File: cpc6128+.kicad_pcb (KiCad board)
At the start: 2 copper layers, 284 x 140.5 mm, 194 parts, among them IC101 AMS40489, IC102 z80_6128, IC103 SED9420Cac, IC104 UPD765AC-2, IC105 74LS38, IC106 74LS38, IC107 74HC14, IC108 MC74HC4051N, IC109 LA6393D, IC110 41464, IC111 41464, IC112 41464, IC113 41464, IC114 AY38912, IC115 AMS40464, IC116 74HCT02, J101 rj12, J102 audio/video, J103 Jack audio, J104 Jack Power, Q101 KTC1815Y, Q103 KTC1815Y, Q104 KTC1815Y, Q105 KTC1815Y, Q106 KTC1815Y, Q107 KTC1815Y, SW1 SW_DIP_x01, X181 40MhZ

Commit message: more accurate on pins definition, power, centronic 36, jack, and some wiring
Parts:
- added C151: 47uF 16V, Capacitor_THT:CP_Radial_D5.0mm_P2.50mm, F.Cu at (218.0, 138.2)
- added L101: ESD-R-12C, cpc6128+:L_Toroid_Vertical_L17_P17, F.Cu at (252.0, 49.2)
- added NC?: nc_db9, cpc6128+:nc_db9, F.Cu at (36.8, 98.5)
- added NC?: nc_db25_db15, cpc6128+:nc_db25_db15, F.Cu at (35.8, 63.0)
- added R210: 470k, Resistor_THT:R_Axial_DIN0207_L6.3mm_D2.5mm_P10.16mm_Horizontal, F.Cu at (243.8, 145.0)
- C130, C139: footprint Capacitor_THT:CP_Radial_D8.0mm_P2.50mm -> Capacitor_THT:CP_Radial_D8.0mm_P5.00mm
- C135: footprint Capacitor_THT:CP_Radial_D5.0mm_P2.50mm -> Capacitor_THT:CP_Radial_D8.0mm_P5.00mm
- CD104: footprint Connector_PinSocket_2.54mm:PinSocket_2x13_P2.54mm_Vertical -> Connector_IDC:IDC-Header_2x13_P2.54mm_Vertical
- IC114: footprint Package_DIP:DIP-28_W7.62mm -> Package_DIP:DIP-28_W15.24mm
- J103: footprint Connector_Audio:Jack_3.5mm_CUI_SJ1-3533NG_Horizontal -> cpc6128+:Jack_6128
- J104: value Jack Power -> POWER_JACK_6128; footprint Connector_BarrelJack:BarrelJack_CUI_PJ-102AH_Horizontal -> cpc6128+:power_jack_6128
- L104: footprint Inductor_THT:L_Toroid_Horizontal_D7.8mm_P13.00mm_Diameter9-5mm_Amidon-T30 -> cpc6128+:L_Toroid_Vertical_L13_P13
- R182: value pont -> 680
- SW1: footprint Connector_PinSocket_1.00mm:PinSocket_1x02_P1.00mm_Vertical -> Connector_PinHeader_2.54mm:PinHeader_1x02_P2.54mm_Vertical
- X181: value 40MhZ -> 40 MHz; footprint Oscillator:Oscillator_DIP-8 -> Oscillator:Oscillator_DIP-14
- moved VR101 48.6 mm to (223.5, 139.0)
- moved J104 11.4 mm to (225.2, 24.8), turned to 0 degrees
- moved L104 8.88 mm to (224.8, 44.0)
- moved D124 7.85 mm to (43.8, 92.5)
- moved NC? 7.81 mm to (37.0, 132.2)
- moved J103 7.43 mm to (27.2, 149.8), turned to 0 degrees
- moved JP102 7.16 mm to (36.0, 92.8)
- moved D125 6.91 mm to (43.8, 102.0)
- moved D126 6.91 mm to (43.8, 106.0)
- moved D127 6.91 mm to (43.8, 111.0)
- moved C114 6.66 mm to (48.5, 97.2)
- moved R195 5.94 mm to (37.0, 154.0), turned to 270 degrees
- moved C125 5.75 mm to (211.5, 67.0), turned to 270 degrees
- moved C138 5.48 mm to (52.2, 145.8), turned to 270 degrees
- moved R113 5.25 mm to (208.5, 68.5), turned to 270 degrees
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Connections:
- C124 pad 1: Net-(C124-Pad1) -> +5V
- IC101 pad 2: Net-(C128-Pad1) -> Net-(IC101-Pad2)
- IC106 pad 14: (no net) -> +5V
- IC107 pad 14: (no net) -> +5V
- J104 pad 2: Net-(C124-Pad1) -> +5V
- J104 pad 3: (no net) -> GND
- LK101 pad 2: (no net) -> GND
- LK102 pad 2: (no net) -> GND
- LK103 pad 2: (no net) -> GND
- LK104 pad 2: (no net) -> GND
- LK105 pad 1: (no net) -> Net-(IC101-Pad119)
- LK105 pad 2: (no net) -> GND
- X181 pad 1: Net-(C128-Pad1) -> Net-(X181-Pad1)
- X181 pad 8: (no net) -> Net-(IC101-Pad2)
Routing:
- net GND: track 504.6 -> 636.3 mm
- net +5V: track 349.3 -> 463.1 mm
- net /video/R: track 19.0 -> 119.8 mm
- net /FloppyDisk/~READY: track 13.2 -> 88.2 mm
- net /FloppyDisk/~WRPT: track 5.55 -> 80.4 mm
- net /FloppyDisk/~SIDE1: track 13.5 -> 88.3 mm
- net /FloppyDisk/~RDDATA: track 13.2 -> 87.7 mm
- net /FloppyDisk/~STEP: track 0.00 -> 56.5 mm, vias 0 -> 1
- net /FloppyDisk/~WGATE: track 0.00 -> 50.7 mm, vias 0 -> 1
- net CLK16: track 19.5 -> 59.2 mm
- net Net-(IC104-Pad29): track 0.00 -> 39.5 mm, vias 0 -> 1
- net Net-(IC104-Pad27): track 2.54 -> 41.2 mm, vias 0 -> 1
- net /FloppyDisk/~TK00: track 13.2 -> 47.0 mm
- net /FloppyDisk/~DSEL: track 44.6 -> 78.4 mm
- net /FloppyDisk/~WDATA: track 0.00 -> 28.1 mm
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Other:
- board text removed: "Molex"

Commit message: finished the centronic 36, some more refinements on placement, new footprint for some connectors
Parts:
- CD104: footprint Connector_IDC:IDC-Header_2x13_P2.54mm_Vertical -> cpc6128+:Connector_Disk_2x13
- CP101, CP102: footprint Connector_PinSocket_2.00mm:PinSocket_2x09_P2.00mm_Vertical -> cpc6128+:CP01_02
- CP103: footprint Connector_PinSocket_1.27mm:PinSocket_1x10_P1.27mm_Vertical -> cpc6128+:CP_103_104
- CP104: value Conn 10 -> clavier; footprint Connector_PinSocket_1.27mm:PinSocket_1x10_P1.27mm_Vertical -> cpc6128+:CP_103_104
- CP107: footprint Connector_PinHeader_1.00mm:PinHeader_1x08_P1.00mm_Vertical -> cpc6128+:CP_107
- moved D201 52.0 mm to (238.5, 59.5)
- moved D202 46.2 mm to (247.2, 68.0)
- moved D128 39.3 mm to (238.4, 63.6)
- moved D129 39.3 mm to (238.4, 67.9)
- moved D130 39.3 mm to (247.3, 63.6)
- moved VR101 19.7 mm to (243.1, 141.0)
- moved CD104 14.8 mm to (226.5, 93.2)
- moved CP103 12.8 mm to (156.5, 153.8), turned to 0 degrees
- moved CP104 12.4 mm to (156.2, 150.2), turned to 180 degrees
- moved CP102 6.58 mm to (76.2, 91.8)
- moved CP101 5.74 mm to (77.0, 140.2)
- moved CP107 4.10 mm to (223.8, 132.4)
- moved Q105 3.78 mm to (213.0, 51.5)
- moved D111 2.50 mm to (208.5, 56.8)
- moved CD103 2.46 mm to (225.2, 65.2)
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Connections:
- net /video/X1 renamed X1
- net /video/X2 renamed X2
- net /video/X3 renamed X3
- net /video/X4 renamed X4
- net /video/X5 renamed X5
- net /video/X6 renamed X6
- net /video/X7 renamed X7
- net /video/X8 renamed X8
- C124 pad 1: +5V -> Net-(C124-Pad1)
- CP104 pad 1: /video/Y1 -> Y1
- CP104 pad 10: /video/Y10 -> Y10
- CP104 pad 2: /video/Y2 -> Y2
- CP104 pad 3: /video/Y3 -> Y3
- CP104 pad 4: /video/Y4 -> Y4
- CP104 pad 5: /video/Y5 -> Y5
- CP104 pad 6: /video/Y6 -> Y6
- CP104 pad 7: /video/Y7 -> Y1
- CP104 pad 8: /video/Y8 -> Y8
- CP104 pad 9: /video/Y9 -> Y9
- IC106 pad 14: +5V -> (no net)
- IC107 pad 14: +5V -> (no net)
- IC114 pad 21: /video/PA7 -> PA7
- IC114 pad 22: /video/PA6 -> PA6
- IC114 pad 23: /video/PA5 -> PA5
- IC114 pad 24: /video/PA4 -> PA4
- IC114 pad 25: /video/PA3 -> PA3
- IC114 pad 26: /video/PA2 -> PA2
- IC114 pad 27: /video/PA1 -> PA1
- IC114 pad 28: /video/PA0 -> PA0
- J104 pad 2: +5V -> Net-(C124-Pad1)
- L101 pad 2: +5V -> Net-(C124-Pad1)
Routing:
- net /FloppyDisk/~DSEL: track 78.4 -> 305.2 mm, vias 2 -> 4
- net Y1: track 0.00 -> 130.1 mm
- net ~MOTOR: track 80.5 -> 185.2 mm, vias 2 -> 4
- net /FloppyDisk/~READY: track 88.2 -> 186.2 mm, vias 0 -> 1
- net /FloppyDisk/~TK00: track 47.0 -> 143.4 mm, vias 0 -> 1
- net /FloppyDisk/~WGATE: track 50.7 -> 146.2 mm, vias 1 -> 2
- net /FloppyDisk/~SIDE1: track 88.3 -> 180.6 mm, vias 1 -> 2
- net /FloppyDisk/~RDDATA: track 87.7 -> 177.4 mm, vias 0 -> 1
- net /FloppyDisk/~WDATA: track 28.1 -> 116.4 mm, vias 0 -> 1
- net /FloppyDisk/~WRPT: track 80.4 -> 166.4 mm, vias 0 -> 1
- net /FloppyDisk/~STEP: track 56.5 -> 140.6 mm, vias 1 -> 2
- net /FloppyDisk/~INDEX: track 5.55 -> 87.0 mm, vias 0 -> 2
- net GND: track 636.3 -> 704.7 mm
- net Y2: track 0.00 -> 68.3 mm
- net Y3: track 0.00 -> 67.3 mm
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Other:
- board text added: "CP103"
- board text added: "CP104"
- board text removed: "R182 = pont"

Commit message: Cabled the keyboard
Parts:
- moved C104 6.52 mm to (120.5, 100.8), turned to 180 degrees
- moved R197 5.05 mm to (59.3, 151.2), turned to 270 degrees
- moved R198 5.05 mm to (61.7, 151.2), turned to 270 degrees
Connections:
- NR102 pad 2: Net-(NR102-Pad2) -> X8
- NR102 pad 3: Net-(NR102-Pad3) -> X7
- NR102 pad 4: Net-(NR102-Pad4) -> X6
- NR102 pad 5: Net-(NR102-Pad5) -> X5
- NR102 pad 6: Net-(NR102-Pad6) -> X4
- NR102 pad 7: Net-(NR102-Pad7) -> X3
- NR102 pad 8: Net-(NR102-Pad8) -> X2
- NR102 pad 9: Net-(NR102-Pad9) -> X1
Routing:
- net GND: track 704.7 -> 906.1 mm, vias 2 -> 3
- net X1: track 0.00 -> 130.7 mm
- net X2: track 0.00 -> 125.8 mm, vias 0 -> 2
- net X3: track 0.00 -> 121.3 mm, vias 0 -> 2
- net X4: track 0.00 -> 116.4 mm, vias 0 -> 2
- net X5: track 0.00 -> 109.9 mm
- net X6: track 0.00 -> 105.3 mm
- net X7: track 0.00 -> 101.1 mm
- net X8: track 0.00 -> 97.0 mm
- net Y10: track 58.3 -> 119.8 mm, vias 0 -> 1
- net +5V: track 485.6 -> 502.0 mm

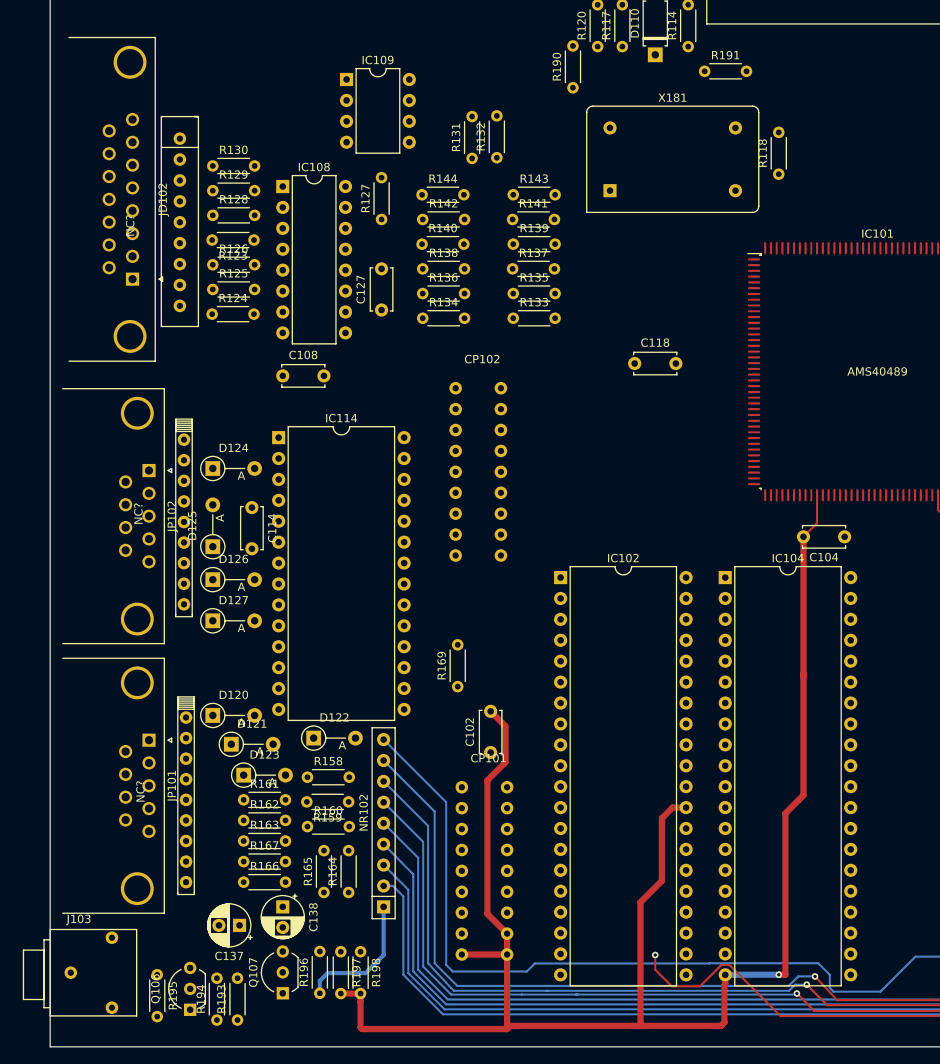
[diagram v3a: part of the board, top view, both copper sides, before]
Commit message: 29-03-2021 : first usage of hierarchical labels. focus on CPU/ Cartridge Connector
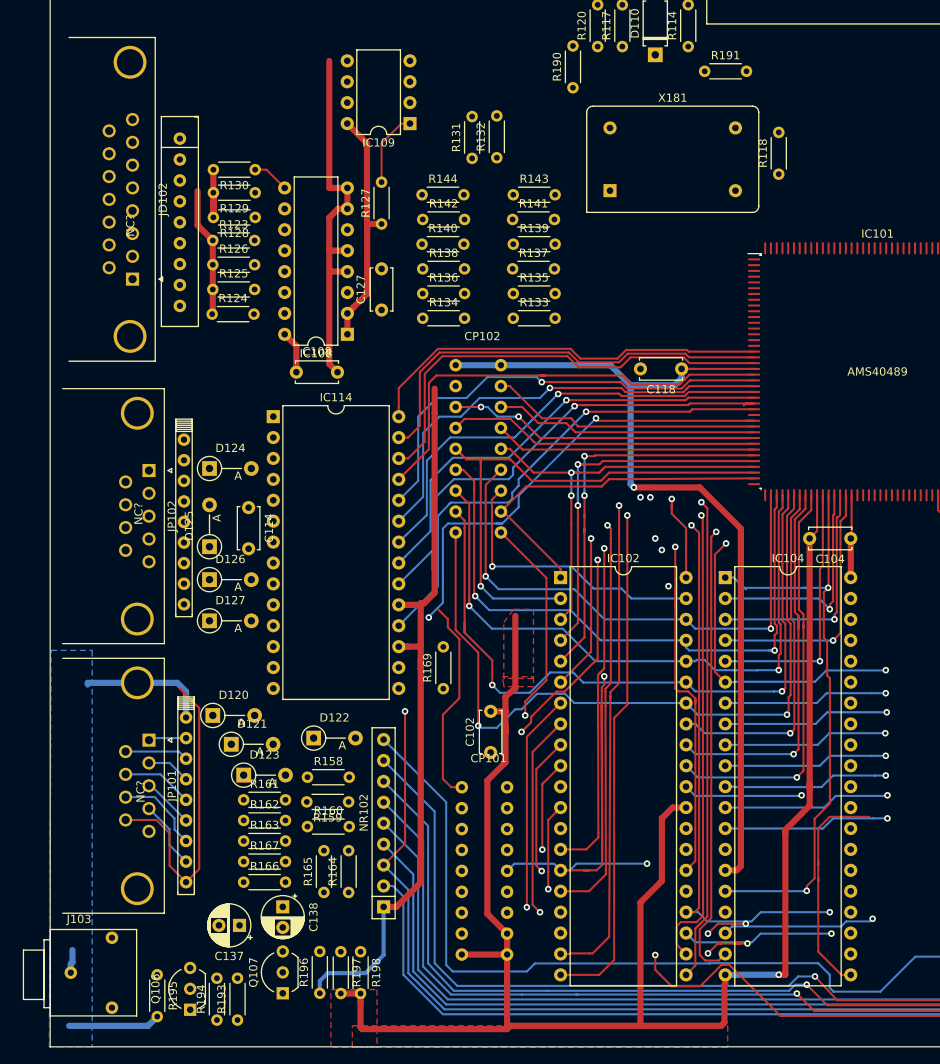
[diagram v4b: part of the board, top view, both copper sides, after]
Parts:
- moved IC108 19.6 mm to (60.1, 76.2), turned to 180 degrees
- moved IC109 9.38 mm to (67.7, 50.6), turned to 180 degrees
- moved C118 5.74 mm to (100.7, 80.4), turned to 180 degrees
- moved R130 5.17 mm to (48.9, 56.2), turned to 180 degrees
- moved R128 5.16 mm to (48.9, 62.0), turned to 180 degrees
- moved R129 5.16 mm to (48.9, 59.0), turned to 180 degrees
- moved R123 5.00 mm to (43.8, 64.8), turned to 0 degrees
- moved CP102 2.80 mm to (76.2, 89.0)
- moved IC114 2.63 mm to (51.1, 86.2)
- moved R169 1.77 mm to (71.8, 119.2)
- moved C108 1.71 mm to (53.9, 80.8)
- moved C104 0.78 mm to (121.2, 101.0)
- moved R127 0.55 mm to (64.2, 62.8)
- moved C114 0.40 mm to (48.1, 97.2)
- moved D124 0.40 mm to (43.4, 92.5)
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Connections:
- net Net-(IC101-Pad59) renamed CRDDTA
- IC101 pad 30: Net-(IC101-Pad30) -> CA18
- IC101 pad 31: Net-(IC101-Pad31) -> CA17
- IC101 pad 32: Net-(IC101-Pad32) -> CA16
- IC101 pad 33: Net-(IC101-Pad33) -> CA15
- IC101 pad 34: Net-(IC101-Pad34) -> CA14
- IC101 pad 35: Net-(IC101-Pad35) -> A15
- IC101 pad 36: Net-(IC101-Pad36) -> A14
- IC101 pad 37: Net-(IC101-Pad37) -> A13
- IC101 pad 38: Net-(IC101-Pad38) -> A12
- IC101 pad 39: Net-(IC101-Pad39) -> A11
- IC101 pad 40: Net-(IC101-Pad40) -> A10
- IC101 pad 41: Net-(IC101-Pad41) -> A9
- IC101 pad 42: Net-(IC101-Pad42) -> A8
- IC101 pad 43: Net-(IC101-Pad43) -> A7
- IC101 pad 44: Net-(IC101-Pad44) -> A6
- IC101 pad 45: Net-(IC101-Pad45) -> A5
- IC101 pad 46: Net-(IC101-Pad46) -> A4
- IC101 pad 47: Net-(IC101-Pad47) -> A3
- IC101 pad 48: Net-(IC101-Pad48) -> A2
- IC101 pad 49: Net-(IC101-Pad49) -> A1
- IC101 pad 51: Net-(IC101-Pad51) -> A0
- IC101 pad 53: ~IOR -> /FloppyDisk/~IOR
- IC101 pad 54: ~IOW -> /FloppyDisk/~IOW
- IC101 pad 55: ~FDC -> /FloppyDisk/~FDC
- IC101 pad 58: Net-(IC101-Pad58) -> D7
- IC101 pad 60: Net-(IC101-Pad60) -> D5
- IC101 pad 61: Net-(IC101-Pad61) -> D4
- IC101 pad 62: Net-(IC101-Pad62) -> D3
- IC101 pad 63: Net-(IC101-Pad63) -> D2
- IC101 pad 64: Net-(IC101-Pad64) -> D1
- IC101 pad 65: Net-(IC101-Pad65) -> D0
- IC104 pad 2: NIOR -> /FloppyDisk/~IOR
- IC104 pad 3: NIOW -> /FloppyDisk/~IOW
- IC104 pad 4: NFDC -> /FloppyDisk/~FDC
- IC114 pad 15: /video/CLK1 -> CLK1
- IC114 pad 16: /video/~RESET -> ~RESET
- IC114 pad 18: /video/PC7 -> PC7
- IC114 pad 20: /video/PC6 -> PC6
- NC? pad 1: (no net) -> Net-(JP101-Pad9)
- NC? pad 2: (no net) -> Net-(JP101-Pad4)
- NC? pad 3: (no net) -> Net-(JP101-Pad8)
- NC? pad 4: (no net) -> Net-(JP101-Pad3)
- NC? pad 5: (no net) -> Net-(JP101-Pad7)
- NC? pad 6: (no net) -> Net-(JP101-Pad2)
- NC? pad 7: (no net) -> Net-(JP101-Pad6)
- NC? pad 8: (no net) -> Net-(JP101-Pad1)
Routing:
- net +5V: track 502.0 -> 749.9 mm, vias 2 -> 3
- net D1: track 0.00 -> 105.0 mm, vias 0 -> 3
- net A4: track 0.00 -> 92.5 mm, vias 0 -> 2
- net GND: track 906.1 -> 992.7 mm
- net A5: track 0.00 -> 86.2 mm, vias 0 -> 2
- net D0: track 0.00 -> 80.1 mm, vias 0 -> 3
- net A6: track 0.00 -> 77.9 mm, vias 0 -> 2
- net A7: track 0.00 -> 77.4 mm, vias 0 -> 2
- net CLK4: track 13.8 -> 88.7 mm, vias 0 -> 2
- net RESET: track 0.00 -> 73.7 mm, vias 0 -> 2
- net A3: track 0.00 -> 69.0 mm, vias 0 -> 2
- net A8: track 0.00 -> 67.4 mm, vias 0 -> 2
- net READY: track 5.75 -> 72.8 mm, vias 1 -> 3
- net A12: track 0.00 -> 66.1 mm, vias 0 -> 1
- net PA5: track 0.00 -> 64.9 mm, vias 0 -> 1
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- added copper zone on B.Cu, net GND
- added copper zone on F.Cu, net GND

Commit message: finished work on Z80
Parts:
- X181: footprint Oscillator:Oscillator_DIP-14 -> cpc6128+:Oscillator_X181_DIP-14
- moved X181 18.6 mm to (92.5, 40.2)
- moved R191 7.03 mm to (110.2, 42.2)
- moved R158 5.05 mm to (60.3, 130.2), turned to 180 degrees
- moved R160 5.05 mm to (60.3, 135.8), turned to 180 degrees
- moved R118 3.03 mm to (115.5, 56.4)
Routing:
- net (no net): track 93.0 -> 214.8 mm, vias 11 -> 12
- net D2: track 30.7 -> 105.5 mm, vias 2 -> 6
- net CCLR: track 0.00 -> 73.5 mm, vias 0 -> 2
- net SIN: track 0.00 -> 65.4 mm, vias 0 -> 2
- net Y10: track 119.8 -> 179.2 mm
- net A10: track 36.6 -> 79.7 mm, vias 1 -> 2
- net D6: track 31.4 -> 71.8 mm
- net D4: track 46.5 -> 81.3 mm, vias 2 -> 4
- net D1: track 105.0 -> 139.3 mm, vias 3 -> 4
- net D7: track 20.2 -> 54.4 mm
- net /CPU/~NMI: track 8.89 -> 42.9 mm, vias 1 -> 2
- net D5: track 36.9 -> 70.0 mm
- net D3: track 44.7 -> 76.5 mm
- net /CPU/~MI: track 0.00 -> 30.7 mm, vias 0 -> 1
- net /CPU/~RFSH: track 0.00 -> 30.5 mm, vias 0 -> 1
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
